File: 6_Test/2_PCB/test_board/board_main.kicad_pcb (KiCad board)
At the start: 4 copper layers, 105.5 x 83 mm, 81 parts, among them J1 PWR_Supply_Pins, J10 Chip_AVSS_GND_Jumpers, J11 Buffer_PWR_Jumper, J12 Reset_PWR_Jumpers, J13 Reset_Signal_Jumpers, J14 1546551-4, J2 Analog_Input_Pins, J3 Digital_Input_Pins, J4 Digital_Output_Pins, J5 Chip_VDD_Jumpers, J6 BNC_Odd, J7 BNC_Even, J8 BNC_Jumpers, J9 Analog_Input_Jumpers, U1 TPS74501PDRVR, U2 ADA4807-1AKSZ-R7, U3 ADA4807-1AKSZ-R7, U4 TPS74501PDRVR, U5 SN74HC74DR, U6 CD4001BM96, U7 SN74LVC245APWR, U8 SN74LVC245APWR

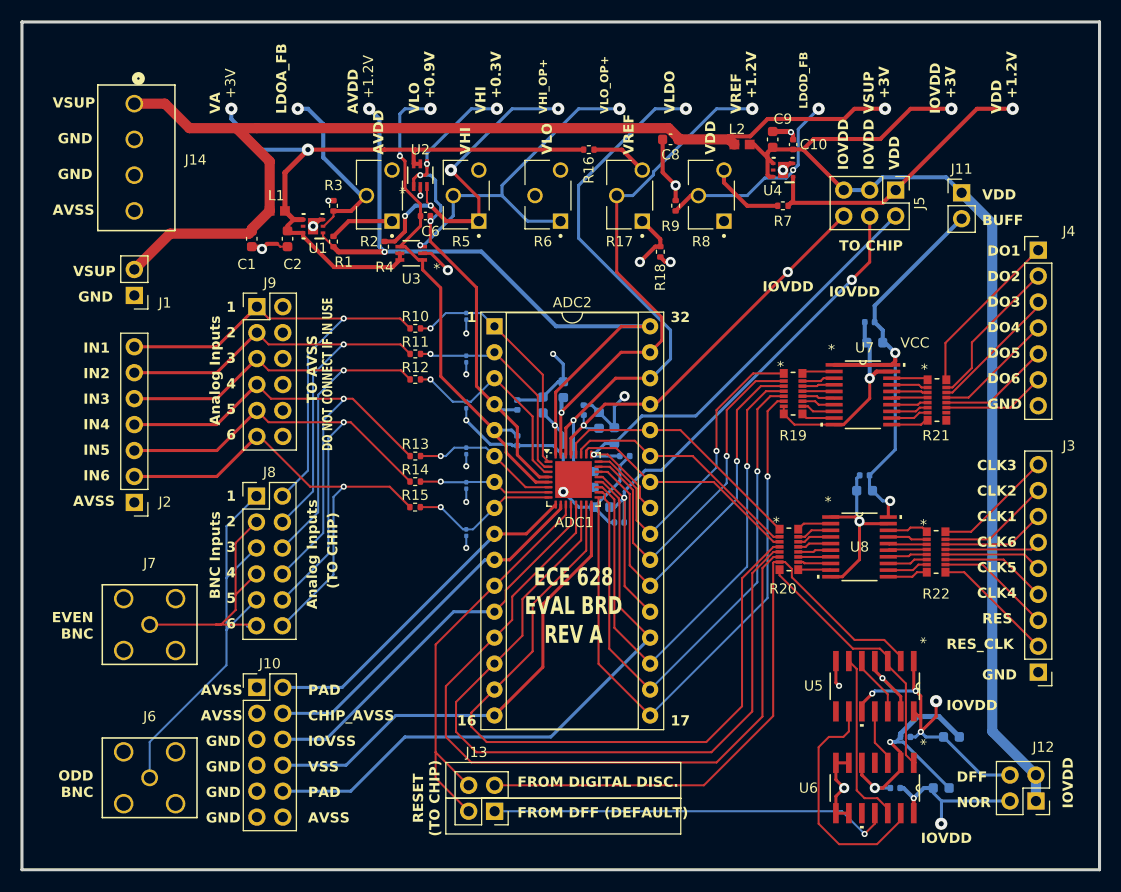
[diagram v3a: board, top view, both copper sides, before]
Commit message: added fiducials on front and back silkscreen and updated fab outputs
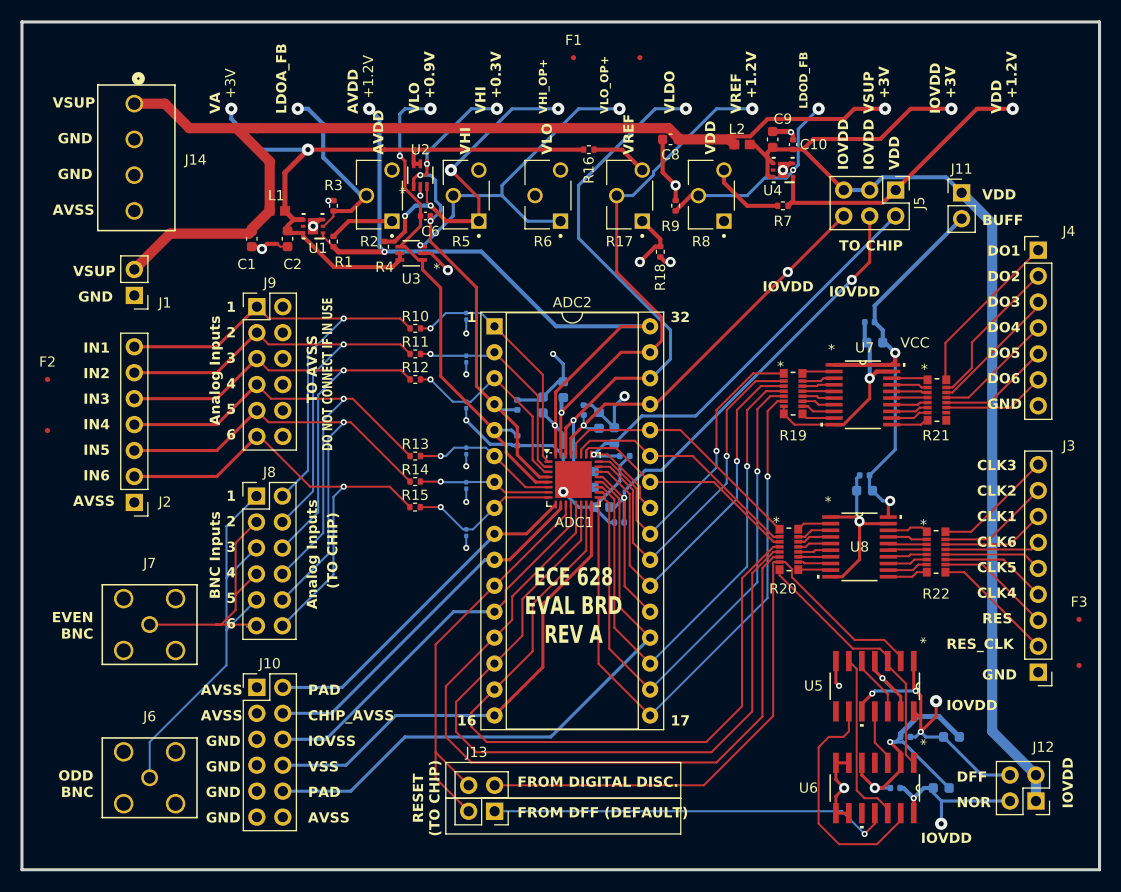
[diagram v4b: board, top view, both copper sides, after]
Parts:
- added F1: Fiducial_0.5mm_Mask1.5mm, Fiducial:Fiducial_0.5mm_Mask1.5mm, F.Cu at (122.0, 61.0)
- added F2: Fiducial_0.5mm_Mask1.5mm, Fiducial:Fiducial_0.5mm_Mask1.5mm, F.Cu at (70.5, 92.5)
- added F3: Fiducial_0.5mm_Mask1.5mm, Fiducial:Fiducial_0.5mm_Mask1.5mm, F.Cu at (171.5, 116.0)
- added F4: Fiducial_0.5mm_Mask1.5mm, Fiducial:Fiducial_0.5mm_Mask1.5mm, F.Cu at (128.5, 61.0)
- added F5: Fiducial_0.5mm_Mask1.5mm, Fiducial:Fiducial_0.5mm_Mask1.5mm, F.Cu at (70.5, 97.5)
- added F6: Fiducial_0.5mm_Mask1.5mm, Fiducial:Fiducial_0.5mm_Mask1.5mm, F.Cu at (171.5, 120.5)
